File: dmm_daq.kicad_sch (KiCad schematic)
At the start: 54 parts, among them K1 G6K-2F-Y-TR, K2 G6K-2F-Y-TR, K3 G6K-2F-Y-TR, K4 G6K-2F-Y-TR, U1 HY3131, X1 4.9152MHz

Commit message: Board is fully routed
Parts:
- R28: value 910 -> 910m
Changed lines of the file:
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@@
       (effects (font (size 1.27 1.27)) (justify right bottom))
     )
-    (property "Value" "910" (at 148.59 130.81 0)
+    (property "Value" "910m" (at 148.59 130.81 0)
       (effects (font (size 1.27 1.27)) (justify left bottom))
     )

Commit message: Step and gerber files added
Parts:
- R12: Tolerabce 1% -> (none)
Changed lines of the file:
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@@
       (effects (font (size 1.27 1.27)) hide)
-    )
-    (property "Tolerabce" "1%" (at 133.35 68.58 0)
-      (effects (font (size 1.27 1.27)) (justify left) hide)
     )
     (property "Tolerance" "1%" (at 132.08 68.58 0)

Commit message: Added galvanic isolation
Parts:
- removed R32: 33, Resistor_SMD:R_0603_1608Metric, symbol res_0603:33
- C1, C3: value 5p -> 5p1; symbol cap_0603:5p -> cap_0603:5p1; MFG NAME Kyocera AVX -> Yageo; MFG PN 06035A5R0BAT2A -> CC0603CRNPO9BN5R1
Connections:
- net GND is gone; now on net VSSA: C12.1, C7.1, C8.1, U1.35 (VSS)
- net CurrentIn: now also K1.5 (NO2); no longer K1.4 (NO1)
- net DMM_IN: now also K1.6 (COM2); no longer K1.3 (COM1)
- net MISO: now also U1.32 (DO)
- net VdOhmCap: now also K1.7 (NC2); no longer K1.2 (NC1)

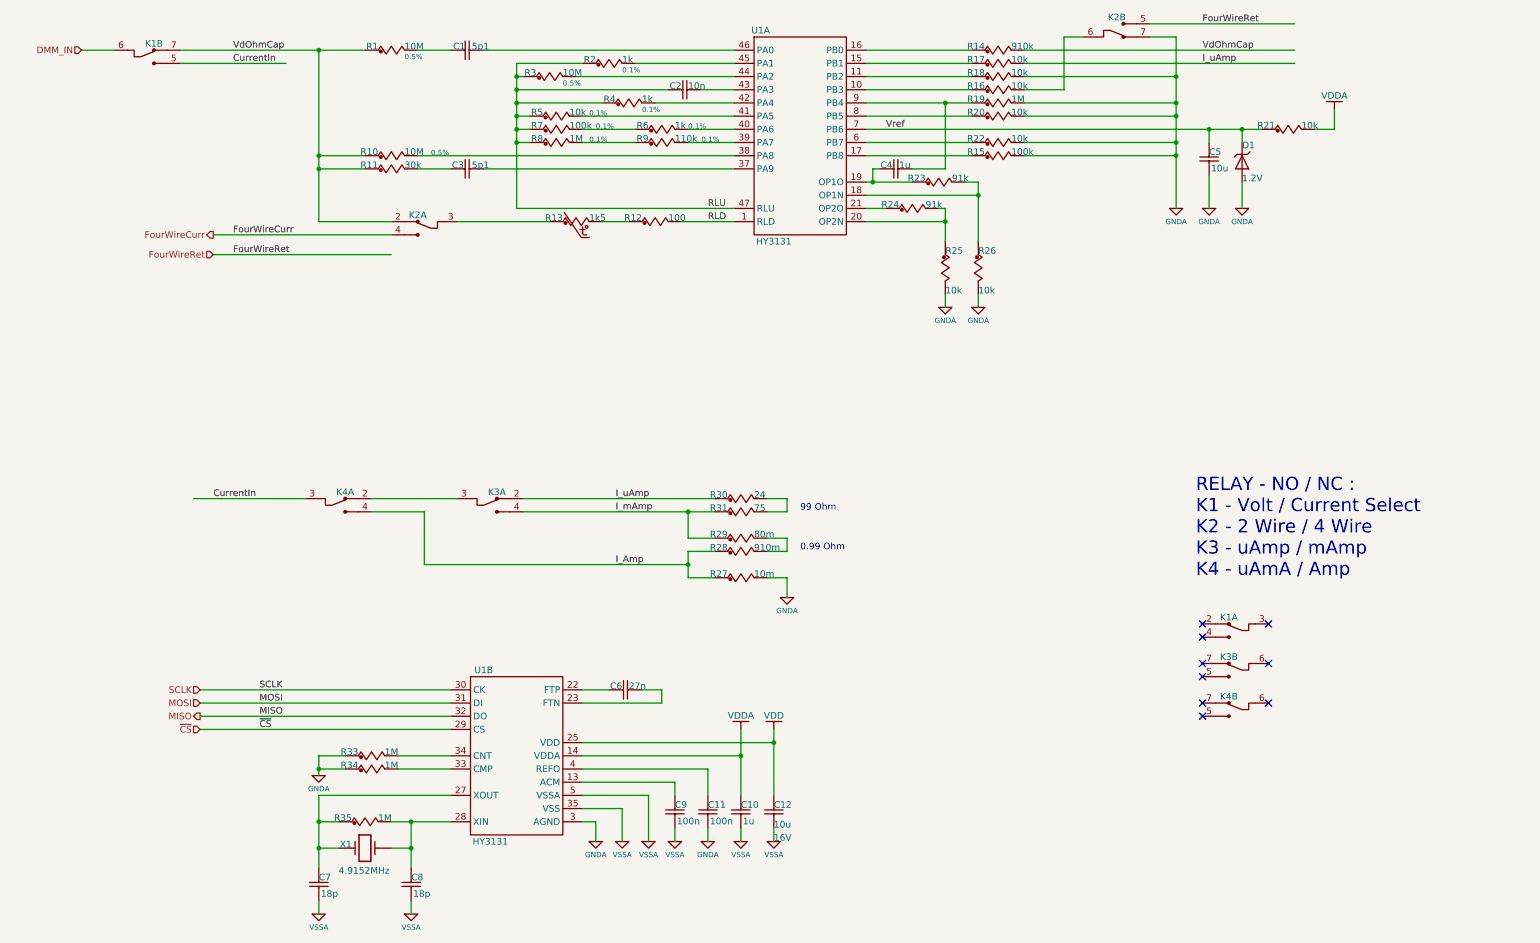
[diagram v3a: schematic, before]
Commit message: Schematics updated with current protection and EEPROM
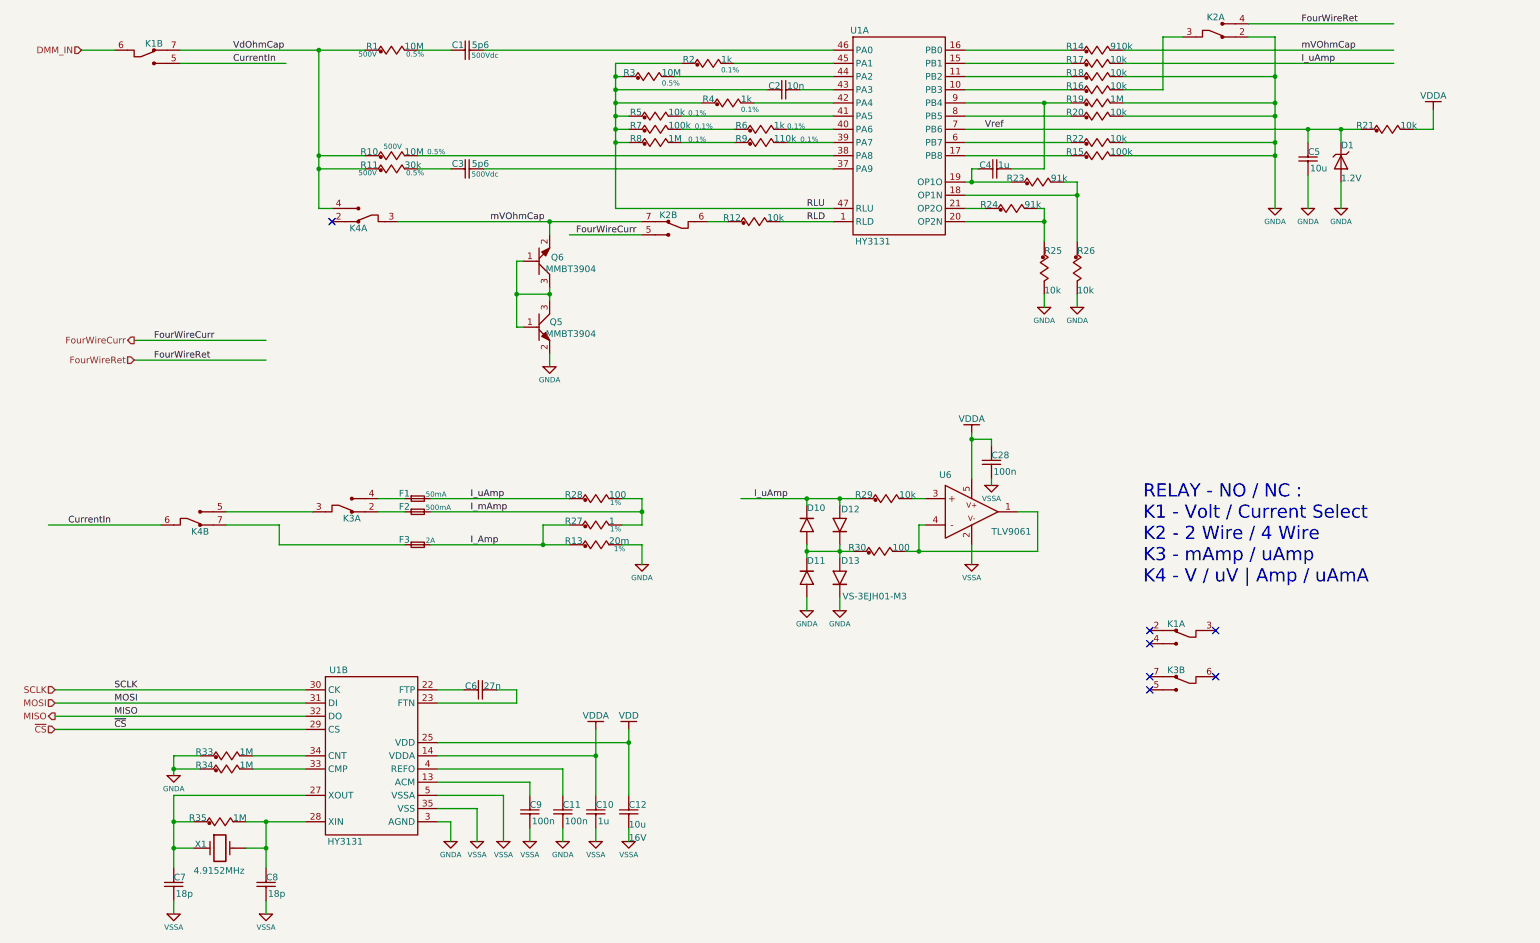
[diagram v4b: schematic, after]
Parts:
- removed C1, C3: 5p1, Capacitor_SMD:C_0603_1608Metric, symbol cap_0603:5p1
- removed R1, R10: 10M, Resistor_SMD:R_0603_1608Metric, symbol res_0603:10M_05%
- removed R11: 30k, Resistor_SMD:R_0603_1608Metric, symbol res_0603:30k
- removed R12: 100, Resistor_SMD:R_0603_1608Metric, symbol res_0603:100
- removed R13: 1k5, Resistor_SMD:R_0805_2012Metric, symbol res_0805:ptc_1k5
- removed R27: 10m, Resistor_SMD:R_0805_2012Metric, symbol res_0805:10m
- removed R28: 910m, Resistor_SMD:R_0805_2012Metric, symbol res_0805:910m
- removed R29: 80m, Resistor_SMD:R_0805_2012Metric, symbol res_0805:80m
- removed R30: 24, Resistor_SMD:R_0805_2012Metric, symbol res_0805:24
- removed R31: 75, Resistor_SMD:R_0805_2012Metric, symbol res_0805:75
- added C1, C3: 5p6, Capacitor_SMD:C_1206_3216Metric, symbol cap_1206:5p6_HV
- added C28: 100n, Capacitor_SMD:C_0603_1608Metric, symbol cap_0603:100n
- added D10, D11, D12, D13: VS-3EJH01-M3, sesa_device:SlimSMPA, symbol sesa_diode:VS-3EJH01-M3
- added F1: 50mA, Fuse:Fuse_1206_3216Metric, symbol sesa_fuse:50mA_PPTC
- added F2: 500mA, Fuse:Fuse_1206_3216Metric, symbol sesa_fuse:500mA_PPTC
- added F3: 2A, Fuse:Fuse_1206_3216Metric, symbol sesa_fuse:2A_PPTC
- added Q5, Q6: MMBT3904, Package_TO_SOT_SMD:SOT-23-3, symbol sesa_transistor:MMBT3904
- added R1, R10: 10M, Resistor_SMD:R_1206_3216Metric, symbol res_1206:10M_HV
- added R11: 30k, Resistor_SMD:R_1206_3216Metric, symbol res_1206:30k_HV
- added R12, R29: 10k, Resistor_SMD:R_0603_1608Metric, symbol res_0603:10k
- added R13: 20m, Resistor_SMD:R_1206_3216Metric, symbol res_1206:20m
- added R27: 1, Resistor_SMD:R_1206_3216Metric, symbol res_1206:1R
- added R28: 100, Resistor_SMD:R_1206_3216Metric, symbol res_1206:100
- added R30: 100, Resistor_SMD:R_0603_1608Metric, symbol res_0603:100
- added U6: TLV9061, Package_TO_SOT_SMD:SOT-23-5, symbol sesa_ic_analog:TLV9061
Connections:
- net CurrentIn: now also K4.6 (COM2); no longer K4.3 (COM1)
- net FourWireCurr: now also K2.5 (NO2); no longer K2.4 (NO1)
- net FourWireRet: now also K2.4 (NO1); no longer K2.5 (NO2)
- net GNDA: now also K2.2 (NC1), D11.2 (A), D13.1 (K), Q5.2 (S), R13.2; no longer K2.7 (NC2)
- net I_Amp: now also F3.2, R13.1, R27.1; no longer K4.4 (NO1)
- net I_mAmp: now also F2.2, R27.2, R28.2; no longer K3.4 (NO1)
- net I_uAmp: now also D10.1 (K), D12.2 (A), F1.2, R28.1, R29.1; no longer K3.2 (NC1)
- net RLD: now also R12.2
- net VDDA: now also C28.2, U6.5 (V+)
- net VSSA: now also C28.1, U6.2 (V-)
- net VdOhmCap: now also K4.4 (NO1), R1.1, R10.1, R11.1; no longer K2.2 (NC1), R14.2
- net at R16.2: now also K2.3 (COM1); no longer K2.6 (COM2)
- net at U1.37 (PA9): now also C3.1
- net at U1.38 (PA8): now also R10.2
- net at U1.46 (PA0): now also C1.1
- net at K3.3 (COM1): now also K4.5 (NO2); no longer K4.2 (NC1)
- net at K4.7 (NC2): now also F3.1
- new net: Q5.1 (G), Q5.3 (D), Q6.1 (G), Q6.3 (D)
- new net: C1.2, R1.2
- new net: F2.1, K3.2 (NC1)
- new net: F1.1, K3.4 (NO1)
- new net: R29.2, U6.3 (IN+)
- new net: R30.2, U6.1 (OUTA), U6.4 (IN-)
- new net: D10.2 (A), D11.1 (K), D12.1 (K), D13.2 (A), R30.1
- new net: K2.6 (COM2), R12.1
- new net: C3.2, R11.2
- new net mVOhmCap: K2.7 (NC2), K4.3 (COM1), Q6.2 (S), R14.2
- no-connect marks 9 -> 7
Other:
- note added: "RELAY - NO / NC : K1 - Volt / Current Select K2 - 2 Wire / 4 Wire K3 - mAmp / uAmp K4 - V / uV | Amp / uAmA"
- note removed: "0.99 Ohm"
- note removed: "99 Ohm"
- note removed: "RELAY - NO / NC : K1 - Volt / Current Select K2 - 2 Wire / 4 Wire K3 - uAmp / mAmp K4 - uAmA / Amp"
- moved on the sheet: C10, C11, C12, C2, C4, C5, C6, C7, C8, C9, D1, K1A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

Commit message: Isolated analog path is fully routed
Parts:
- added F4: 50mA, Fuse:Fuse_1206_3216Metric, symbol sesa_fuse:50mA_PPTC
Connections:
- net CurrentIn: now also K1.4 (NO1); no longer K1.5 (NO2)
- net DMM_IN: now also K1.3 (COM1), K1.6 (COM2); no longer K1.6 (COM2)
- net VdOhmCap: now also K1.2 (NC1); no longer K1.7 (NC2)
- net mVOhmCap: now also F4.1; no longer K2.7 (NC2), Q6.2 (S)
- new net: F4.2, K2.7 (NC2), Q6.2 (S)
- no-connect marks 7 -> 6
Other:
- moved on the sheet: C1, C3, F1, F2, F3

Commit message: 10MOhm resistors partnumber updated
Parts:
- R1, R10: symbol res_1206:10M_HV -> res_1206:10M_1kV; MFG NAME Panasonic -> Vishay; MFG PN ERJ-P08D1004V -> CRMA1206AF10M0DKEF; Voltage 500V -> 1kV
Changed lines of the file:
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@@
 	)
 	(symbol
-		(lib_id "res_1206:10M_HV")
+		(lib_id "res_1206:10M_1kV")
 		(at 73.66 34.29 0)
 		(unit 1)
@@
 			)
 		)
-		(property "Datasheet" "https://industrial.panasonic.com/cdbs/www-data/pdf/RDO0000/AOA0000C331.pdf"
+		(property "Datasheet" "https://www.vishay.com/docs/68043/crma.pdf"
 			(at 81.026 44.958 0)
 			(effects
@@
 			)
 		)
-		(property "Description" "resistor, 1206, 0.66W, 500V, 0.5%"
+		(property "Description" "resistor, 1206, 0.3W, 1kV, 0.5%"
 			(at 79.248 40.894 0)
 			(effects
@@
 			)
 		)
-		(property "MFG PN" "ERJ-P08D1004V"
+		(property "MFG PN" " CRMA1206AF10M0DKEF"
 			(at 78.994 39.116 0)
 			(effects
@@
 			)
 		)
-		(property "MFG NAME" "Panasonic"
+		(property "MFG NAME" "Vishay"
 			(at 78.994 42.926 0)
 			(effects
@@
 			)
 		)
-		(property "Voltage" "500V"
-			(at 74.168 35.052 0)
+		(property "Voltage" "1kV"
+			(at 74.676 35.052 0)
 			(effects
 				(font
@@
 	)
 	(symbol
-		(lib_id "res_1206:10M_HV")
+		(lib_id "res_1206:10M_1kV")
 		(at 73.66 54.61 0)
 		(unit 1)
@@
 			)
 		)
-		(property "Datasheet" "https://industrial.panasonic.com/cdbs/www-data/pdf/RDO0000/AOA0000C331.pdf"
+		(property "Datasheet" "https://www.vishay.com/docs/68043/crma.pdf"
 			(at 81.026 65.278 0)
 			(effects
@@
 			)
 		)
-		(property "Description" "resistor, 1206, 0.66W, 500V, 0.5%"
+		(property "Description" "resistor, 1206, 0.3W, 1kV, 0.5%"
 			(at 79.248 61.214 0)
 			(effects
@@
 			)
 		)
-		(property "MFG PN" "ERJ-P08D1004V"
+		(property "MFG PN" " CRMA1206AF10M0DKEF"
 			(at 78.994 59.436 0)
 			(effects
@@
 			)
 		)
-		(property "MFG NAME" "Panasonic"
+		(property "MFG NAME" "Vishay"
 			(at 78.994 63.246 0)
 			(effects
@@
 			)
 		)
-		(property "Voltage" "500V"
+		(property "Voltage" "1kV"
 			(at 78.994 52.832 0)
 			(effects
